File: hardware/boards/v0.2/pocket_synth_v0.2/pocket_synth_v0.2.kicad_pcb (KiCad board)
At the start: 8 copper layers, 155 x 162 mm, 47 parts, among them J1 Conn_ARM_JTAG_SWD_10, J2 DEVICE, J3 AudioJack3, J4 AudioJack3, J5 AudioJack3, J6 AudioJack3, J7 DISPLAY, J8 Micro_SD_Card_Det2, J9 HOST, SW1 SW_Push, SW2 SW_Push, SW3 SW_Push, SW4 SW_Push, U1 STM32H743XIHx, U3 SDRAM, U4 STM32H753VIHx, U5 W25Q128JVS, Y1 32.768kHz, Y2 HSE

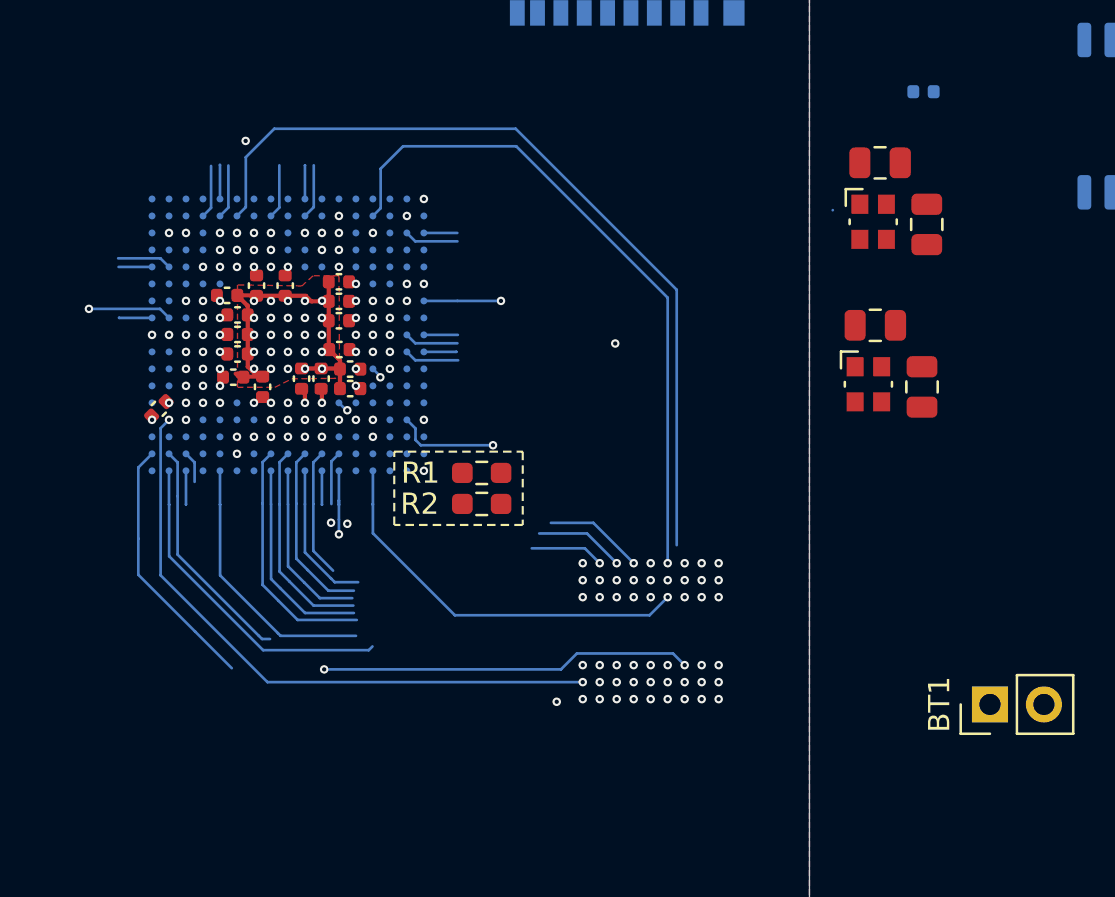
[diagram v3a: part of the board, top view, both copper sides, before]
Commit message: more SDRAM routing
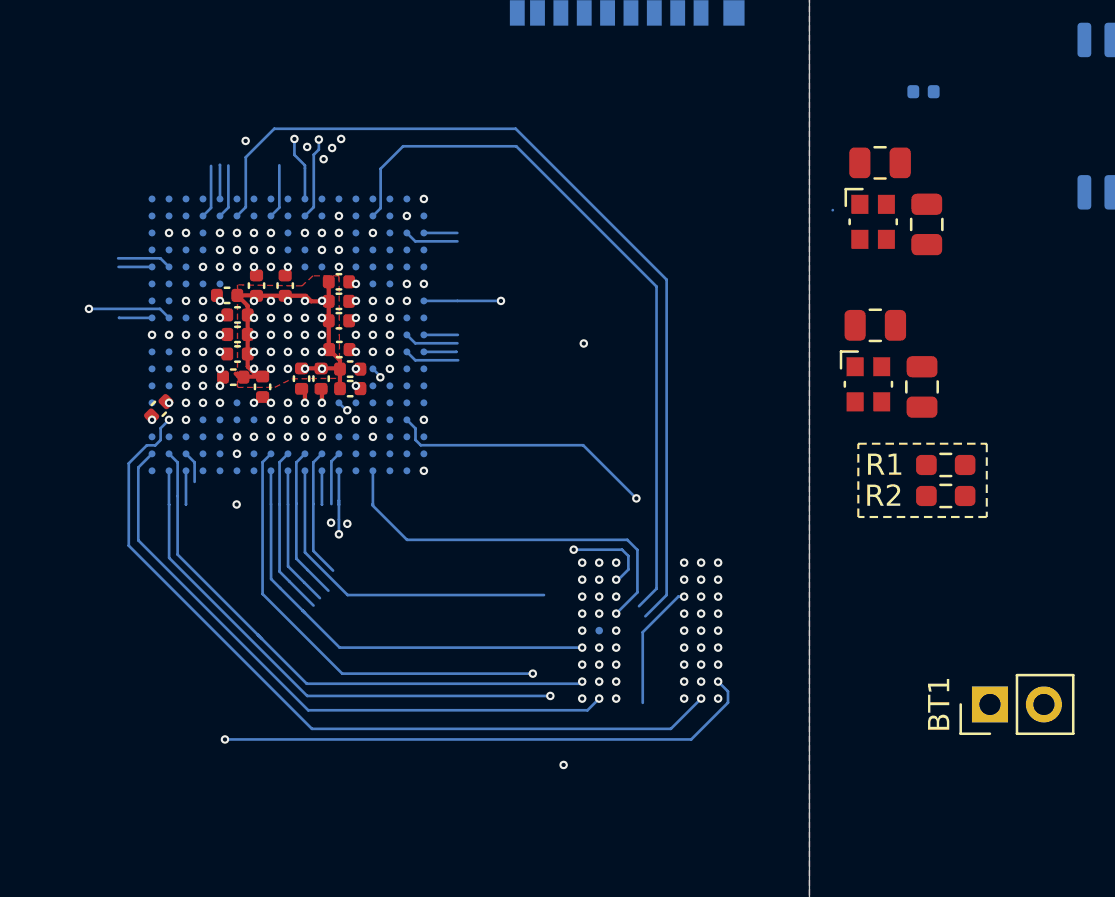
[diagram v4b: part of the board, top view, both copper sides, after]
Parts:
- moved R1 21.9 mm to (95.4, 49.9)
- moved R2 21.9 mm to (95.4, 51.3)
- turned U3 to 0 degrees
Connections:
- U3 pad A2: /FMC_D15 -> /FMC_D14
- U3 pad B1: /FMC_D14 -> /FMC_D15
- U3 pad C2: /FMC_D11 -> /FMC_D10
- U3 pad D1: /FMC_D10 -> /FMC_D11
- U3 pad D2: /FMC_D9 -> /FMC_D8
- U3 pad E1: /FMC_D8 -> /FMC_D9
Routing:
- net /FMC_A12: track 29.6 -> 55.9 mm, vias 2 -> 3
- net /FMC_D6: track 11.2 -> 28.7 mm
- net /FMC_D15: track 10.9 -> 26.8 mm
- net /FMC_SDNE0: track 4.87 -> 19.8 mm
- net /FMC_D14: track 15.7 -> 29.6 mm
- net unconnected-(U1-PH7-PadU13): track 12.5 -> 0.00 mm
- net /FMC_D8: track 13.1 -> 25.3 mm
- net /FMC_D2: track 65.9 -> 53.7 mm
- net /FMC_D9: track 10.5 -> 22.4 mm
- net /FMC_D13: track 15.5 -> 27.3 mm, vias 1 -> 2
- net /FMC_D3: track 62.4 -> 50.8 mm
- net /FMC_D11: track 9.65 -> 21.3 mm
- net /FMC_A7: track 9.00 -> 20.5 mm
- net /FMC_NBL0: track 51.4 -> 40.2 mm
- net /FMC_A8: track 9.52 -> 20.6 mm
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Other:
- board text added: "ER-TFT035-4 OR ER-TFT035-7"

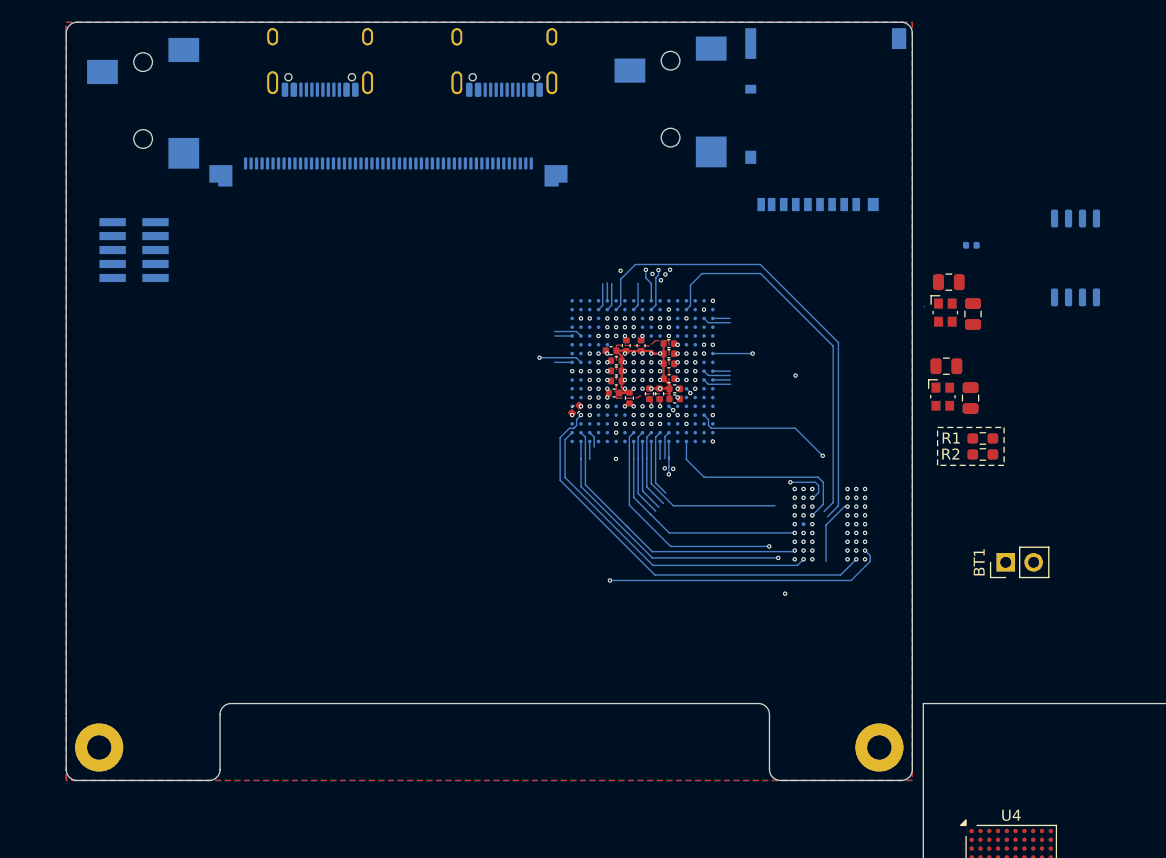
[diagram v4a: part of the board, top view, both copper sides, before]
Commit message: finish routing SDRAM
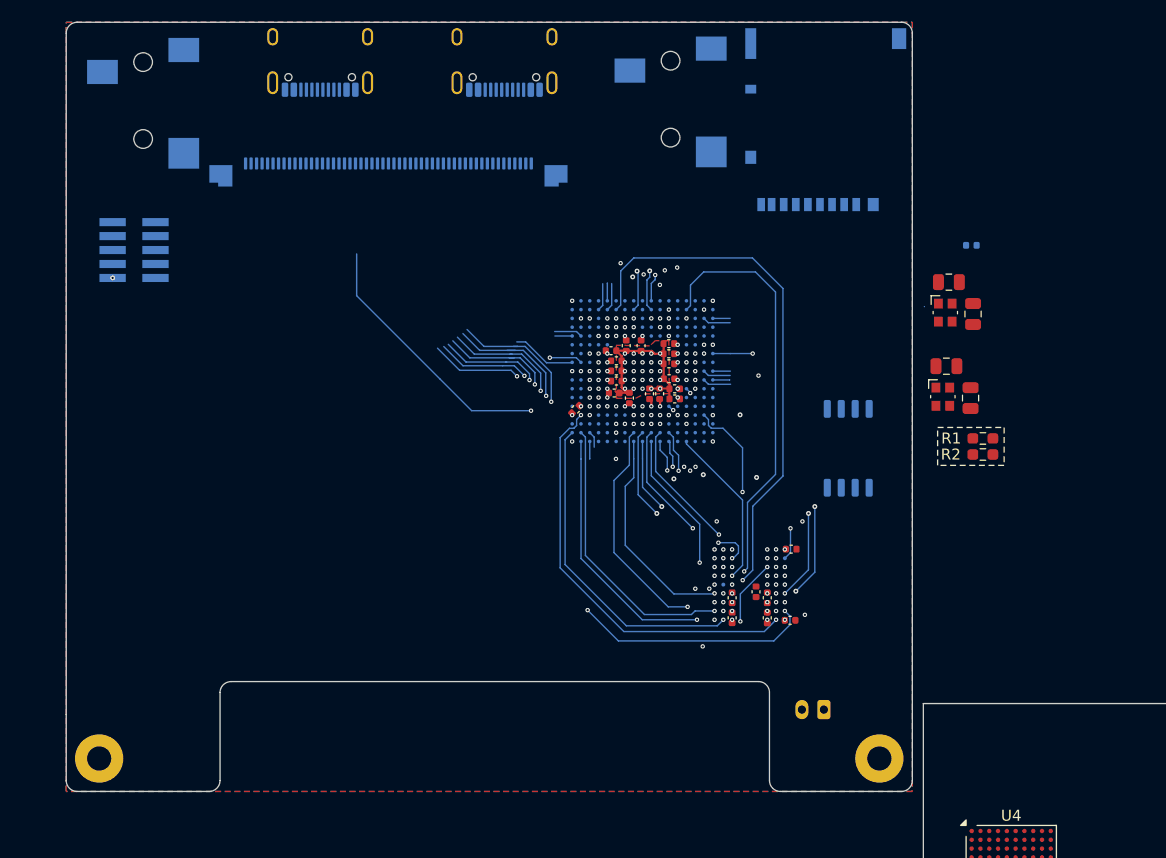
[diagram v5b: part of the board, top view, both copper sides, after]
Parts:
- added C23: 100nf, Capacitor_SMD:C_0402_1005Metric, F.Cu at (74.8, 63.8)
- added C24: 100nf, Capacitor_SMD:C_0402_1005Metric, F.Cu at (77.9, 66.4)
- added C25: 100nf, Capacitor_SMD:C_0402_1005Metric, F.Cu at (78.0, 60.0)
- added C26: 100nf, Capacitor_SMD:C_0402_1005Metric, F.Cu at (72.6, 64.4)
- added C27: 100nf, Capacitor_SMD:C_0402_1005Metric, F.Cu at (72.6, 66.2)
- added C28: 100nf, Capacitor_SMD:C_0402_1005Metric, F.Cu at (75.8, 64.4)
- added C29: 100nf, Capacitor_SMD:C_0402_1005Metric, F.Cu at (75.8, 66.2)
- BT1: footprint Connector_PinHeader_2.54mm:PinHeader_1x02_P2.54mm_Vertical -> Connector_JST:JST_PH_S2B-PH-K_1x02_P2.00mm_Horizontal; moved to B.Cu
- moved U5 27.0 mm to (83.2, 50.8)
- moved BT1 21.3 mm to (81.0, 74.5), turned to 180 degrees
- moved U3 9.14 mm to (74.2, 63.2)
- moved H1 1.00 mm to (15.0, 79.0)
- moved H2 1.00 mm to (86.0, 79.0)
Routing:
- net /LCD_R7: track 3.28 -> 29.5 mm, vias 1 -> 2
- net /FMC_D4: track 6.61 -> 31.2 mm, vias 1 -> 4
- net /FMC_D5: track 7.97 -> 30.2 mm, vias 1 -> 3
- net /FMC_SDNWE: track 5.75 -> 24.6 mm, vias 2 -> 4
- net /FMC_D7: track 10.7 -> 27.5 mm, vias 2 -> 4
- net /FMC_A10: track 7.24 -> 22.4 mm, vias 1 -> 2
- net /FMC_BA1: track 53.1 -> 67.5 mm, vias 2 -> 3
- net /LCD_G1: track 4.91 -> 17.8 mm, vias 1 -> 2
- net /LCD_G0: track 4.17 -> 16.8 mm, vias 1 -> 2
- net /FMC_SDNRAS: track 6.05 -> 18.6 mm, vias 1 -> 2
- net /LCD_G6: track 3.27 -> 15.5 mm, vias 1 -> 2
- net /LCD_G2: track 4.14 -> 16.2 mm, vias 1 -> 2
- net /LCD_G3: track 4.14 -> 16.1 mm, vias 1 -> 2
- net /LCD_G4: track 4.15 -> 15.8 mm, vias 1 -> 2
- net /LCD_G5: track 4.19 -> 15.7 mm, vias 1 -> 2
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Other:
- outline, holes or cut-outs redrawn
- board text added: "BLUETOOTH MODULE FSC-BT1035"
- board text added: "Longest SDRAM trace is 60mm, aim for all traces to have ~20mm skew."

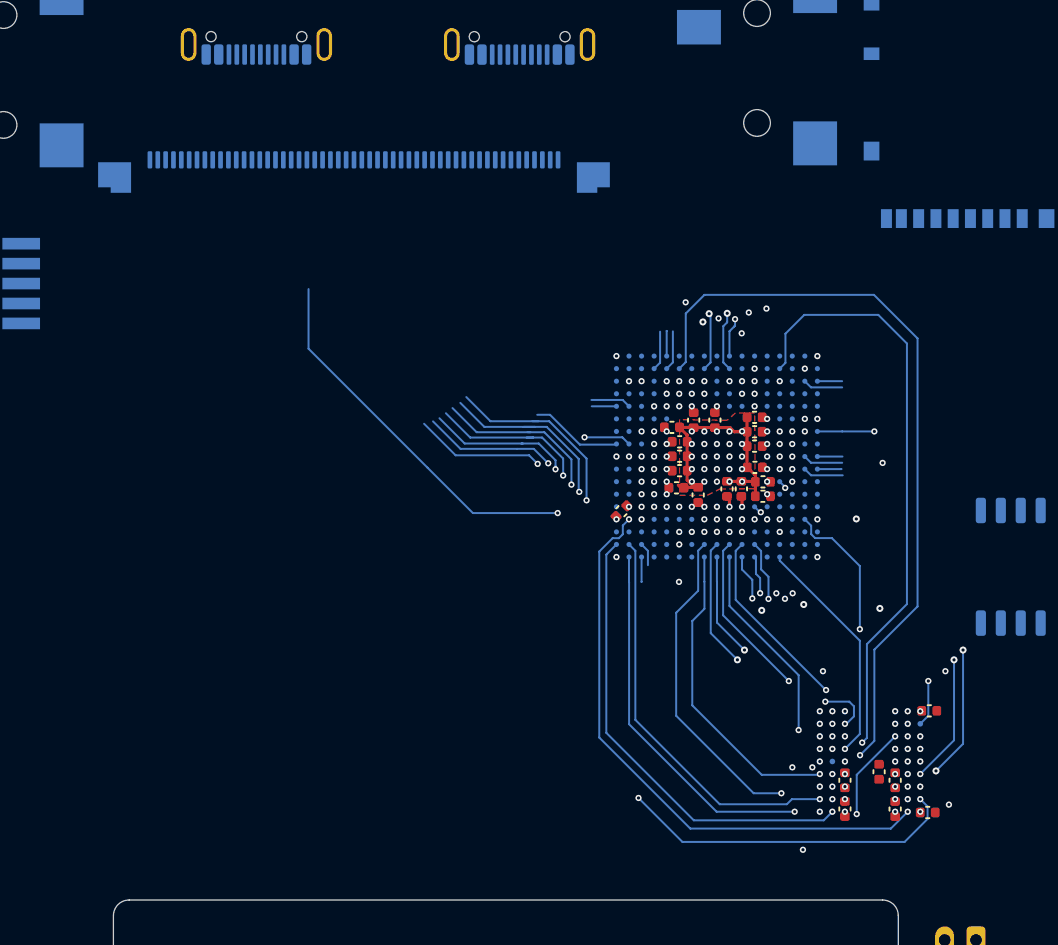
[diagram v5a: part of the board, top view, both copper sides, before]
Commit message: routed display FPC
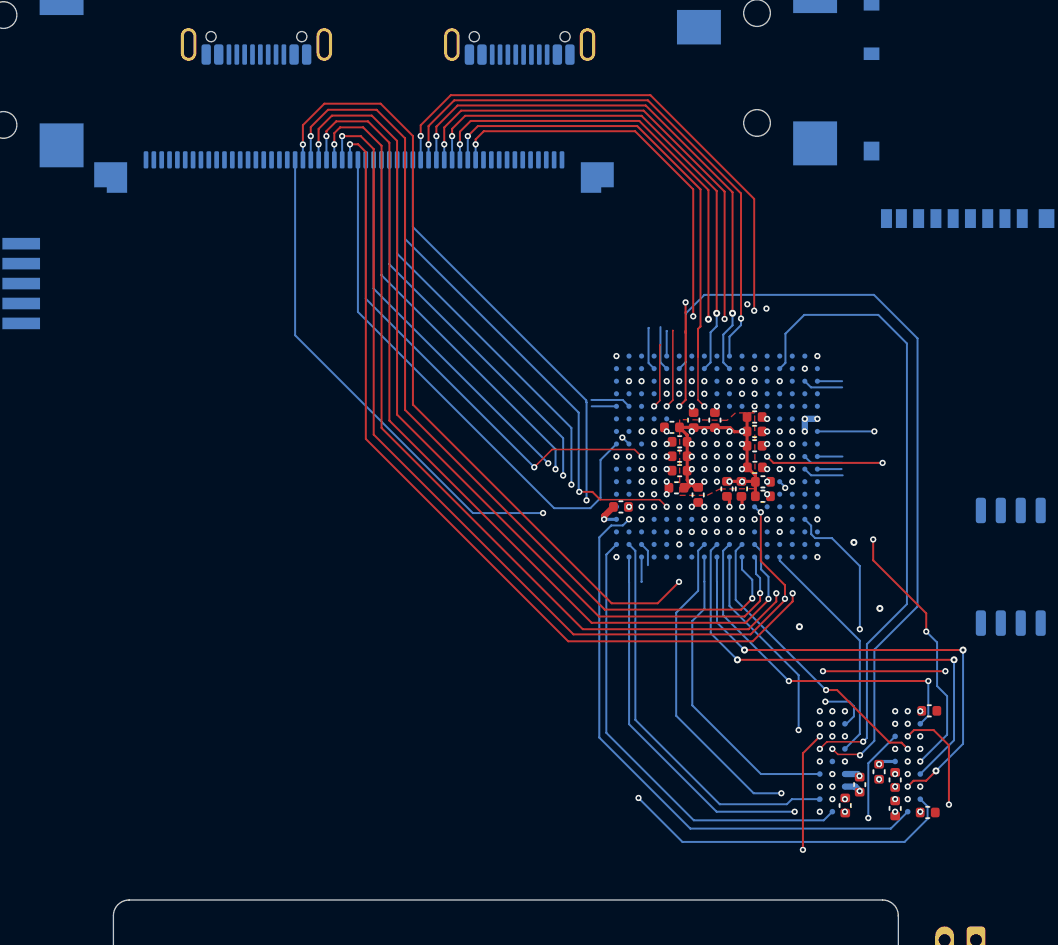
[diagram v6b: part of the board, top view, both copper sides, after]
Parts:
- J7: footprint Connector_FFC-FPC:Amphenol_F32Q-1A7x1-11053_1x53-1MP_P0.5mm_Horizontal -> Connector_FFC-FPC:Amphenol_F32Q-1A7x1-11054_1x54-1MP_P0.5mm_Horizontal
- moved C26 0.98 mm to (73.5, 64.7)
- moved C9 0.27 mm to (58.3, 47.0), turned to 0 degrees
- moved C27 0.22 mm to (72.6, 66.0)
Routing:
- net /LCD_R2: track 5.28 -> 60.3 mm, vias 2 -> 3
- net /LCD_R4: track 2.45 -> 57.2 mm, vias 1 -> 2
- net /LCD_R0: track 5.38 -> 60.0 mm, vias 2 -> 3
- net /LCD_R3: track 3.84 -> 58.3 mm, vias 1 -> 2
- net /LCD_R1: track 6.64 -> 61.2 mm, vias 2 -> 3
- net /LCD_R5: track 2.91 -> 57.2 mm, vias 1 -> 2
- net /LCD_R6: track 3.55 -> 54.1 mm, vias 2 -> 3
- net /LCD_B7: track 4.55 -> 38.9 mm, vias 2 -> 3
- net /LCD_B6: track 2.50 -> 35.9 mm, vias 1 -> 2
- net /LCD_B5: track 3.79 -> 35.5 mm, vias 1 -> 2
- net /LCD_B4: track 4.29 -> 34.7 mm, vias 2 -> 3
- net /LCD_B3: track 3.70 -> 32.8 mm, vias 1 -> 2
- net /LCD_G7: track 5.85 -> 34.5 mm
- net /LCD_B2: track 4.94 -> 32.9 mm, vias 2 -> 3
- net /LCD_B1: track 4.99 -> 32.3 mm, vias 1 -> 2
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- removed copper zone on In6.Cu, net GND
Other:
- copper layers 8 -> 6

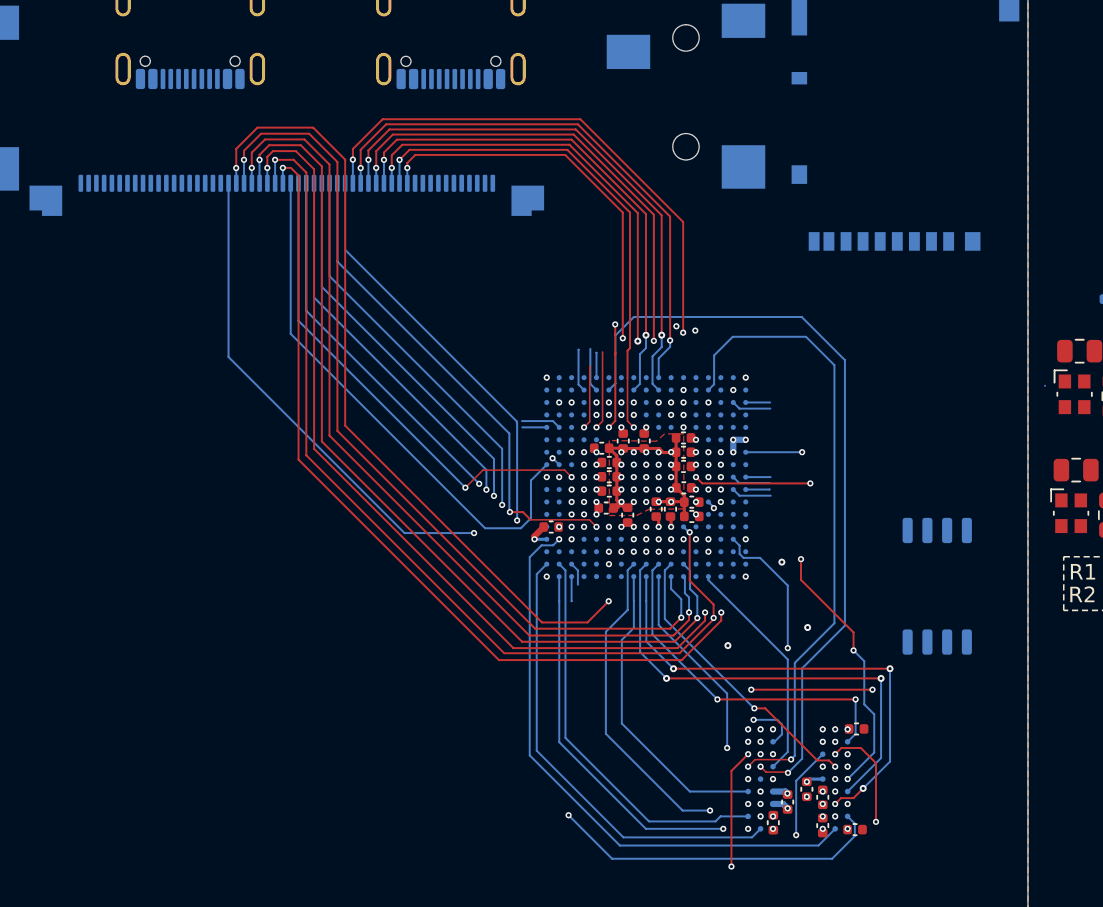
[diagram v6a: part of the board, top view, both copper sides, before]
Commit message: more display connector routing
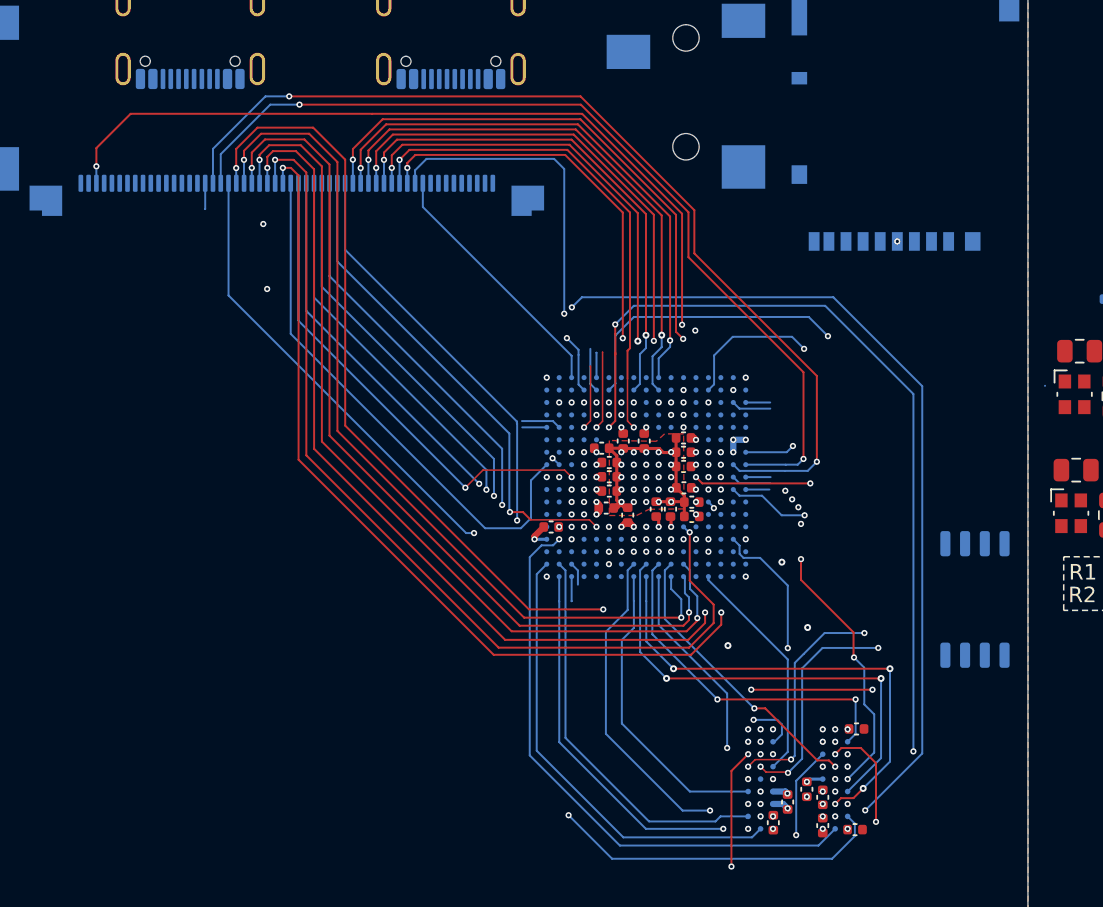
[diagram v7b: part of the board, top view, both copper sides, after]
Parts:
- moved U5 2.57 mm to (85.6, 51.6)
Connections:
- J7 pad 52: unconnected-(J7-Pin_52-Pad52) -> /LCD_DE
- U1 pad A15: unconnected-(U1-PI1-PadA15) -> /LCD_SPI_CLK
- U1 pad A6: unconnected-(U1-VDDLDO-PadA6) -> +3.3V
- U1 pad C14: unconnected-(U1-PI3-PadC14) -> /LCD_SPI_PICO
- U1 pad C17: unconnected-(U1-VDDLDO-PadC17) -> +3.3V
- U1 pad F17: unconnected-(U1-VDD33_USB-PadF17) -> +3.3V
- U1 pad G17: unconnected-(U1-VDD50_USB-PadG17) -> +3.3V
- U1 pad H1: unconnected-(U1-PI12-PadH1) -> /LCD_HSYNC
- U1 pad H2: unconnected-(U1-PI13-PadH2) -> /LCD_VSYNC
- U1 pad L1: unconnected-(U1-VDDA-PadL1) -> VDDA
- U1 pad U12: unconnected-(U1-VDDLDO-PadU12) -> +3.3V
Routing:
- net /LCD_VSYNC: track 0.00 -> 62.8 mm, vias 0 -> 2
- net /LCD_HSYNC: track 0.00 -> 58.9 mm, vias 0 -> 2
- net /LCD_DE: track 6.17 -> 57.1 mm, vias 2 -> 3
- net /SWD_CLK: track 2.75 -> 31.4 mm, vias 0 -> 1
- net /LCD_SPI_PICO: track 0.00 -> 26.6 mm, vias 0 -> 2
- net /SWD_IO: track 3.18 -> 28.2 mm
- net /LCD_SPI_CLK: track 0.00 -> 16.5 mm
- net /FMC_CLK: track 50.1 -> 55.2 mm, vias 2 -> 4
- net /FMC_NBL1: track 40.8 -> 44.2 mm, vias 2 -> 4
- net +3.3V: track 8.38 -> 11.8 mm, vias 29 -> 30
- net /FMC_D2: track 60.6 -> 63.7 mm, vias 2 -> 4
- net /QSPI1_IO3: track 2.58 -> 5.28 mm, vias 0 -> 1
- net /QSPI1_IO1: track 4.16 -> 6.57 mm, vias 1 -> 2
- net /LCD_R7: track 38.1 -> 35.8 mm
- net /QSPI1_CLK: track 3.20 -> 5.13 mm, vias 1 -> 2
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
